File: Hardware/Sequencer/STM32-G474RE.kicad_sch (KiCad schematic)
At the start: 1 part, among them U301 STM32G474RETx

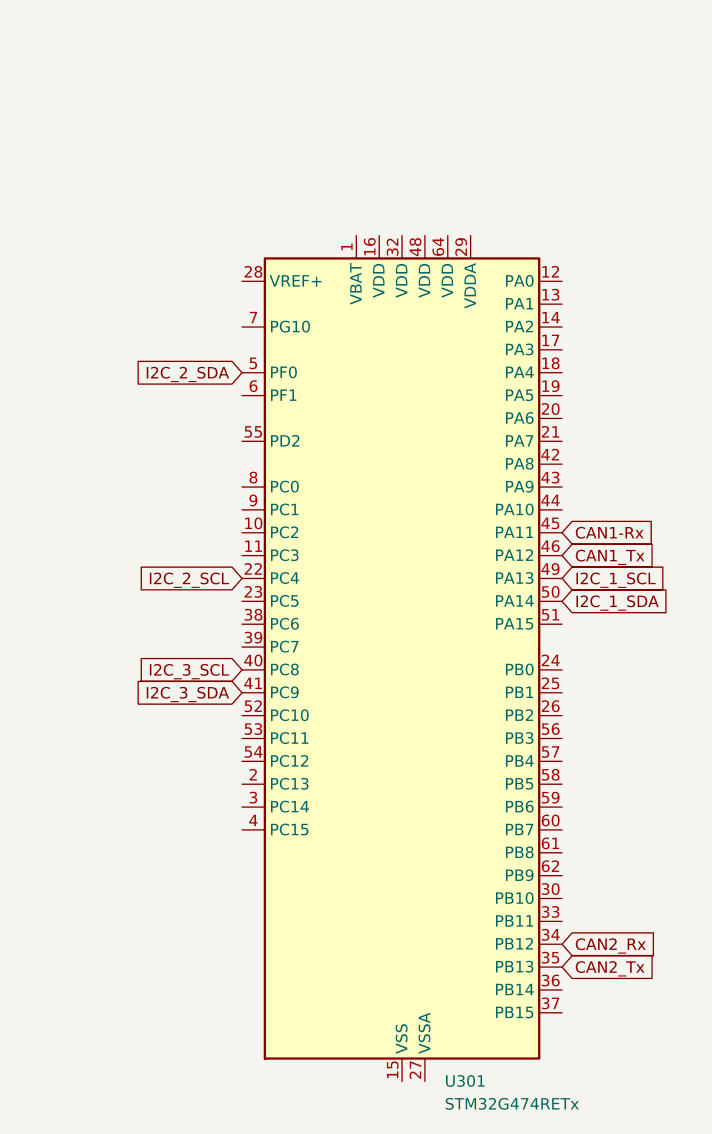
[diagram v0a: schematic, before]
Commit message: Update STM32-G474RE.kicad_sch
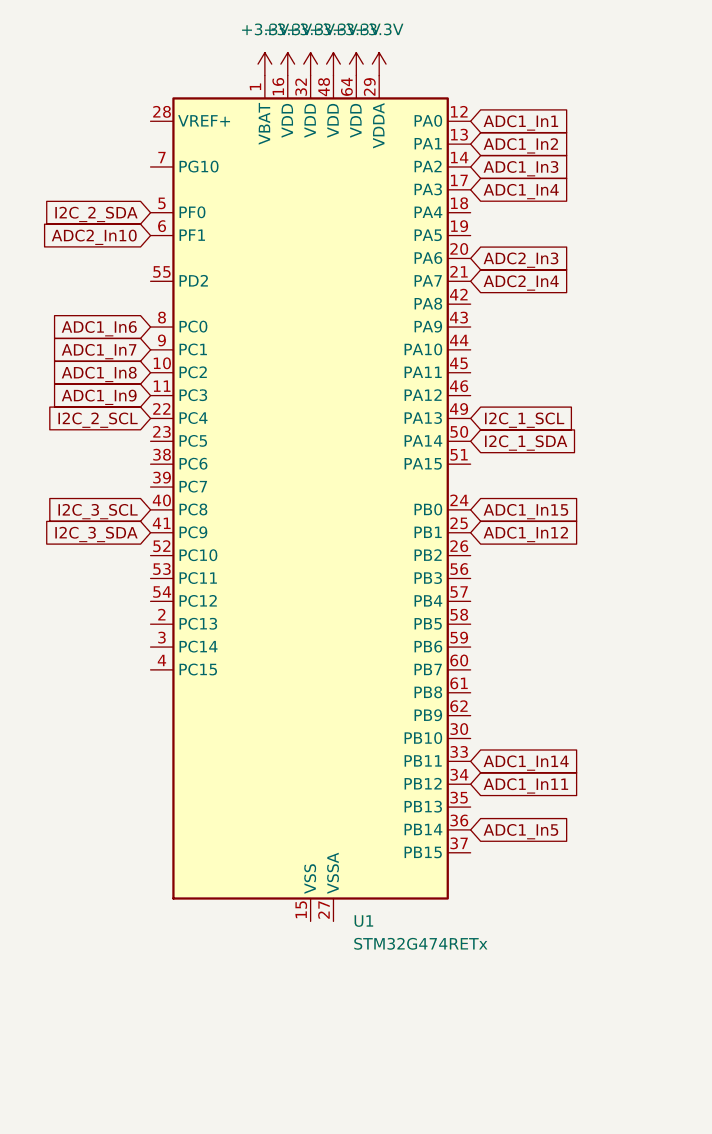
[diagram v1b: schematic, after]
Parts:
- removed U301: STM32G474RETx, Package_QFP:LQFP-64_10x10mm_P0.5mm, symbol MCU_ST_STM32G4:STM32G474RETx
- added U1: STM32G474RETx, Package_QFP:LQFP-64_10x10mm_P0.5mm, symbol MCU_ST_STM32G4:STM32G474RETx
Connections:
- net I2C_1_SCL: now also U1.49 (PA13)
- net I2C_1_SDA: now also U1.50 (PA14)
- net I2C_2_SCL: now also U1.22 (PC4)
- net I2C_2_SDA: now also U1.5 (PF0)
- net I2C_3_SCL: now also U1.40 (PC8)
- net I2C_3_SDA: now also U1.41 (PC9)
- new net: U1.15 (VSS), U1.31 (VSS), U1.47 (VSS), U1.63 (VSS)
- new net +3.3V: U1.1 (VBAT), U1.16 (VDD), U1.29 (VDDA), U1.32 (VDD), U1.48 (VDD), U1.64 (VDD)
- new net ADC1_In1: U1.12 (PA0)
- new net ADC1_In11: U1.34 (PB12)
- new net ADC1_In12: U1.25 (PB1)
- new net ADC1_In14: U1.33 (PB11)
- new net ADC1_In15: U1.24 (PB0)
- new net ADC1_In2: U1.13 (PA1)
- new net ADC1_In3: U1.14 (PA2)
- new net ADC1_In4: U1.17 (PA3)
- new net ADC1_In5: U1.36 (PB14)
- new net ADC1_In6: U1.8 (PC0)
- new net ADC1_In7: U1.9 (PC1)
- new net ADC1_In8: U1.10 (PC2)
- new net ADC1_In9: U1.11 (PC3)
- new net ADC2_In10: U1.6 (PF1)
- new net ADC2_In3: U1.20 (PA6)
- new net ADC2_In4: U1.21 (PA7)

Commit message: Beaucoup de changements sur le pcb
Alim corrigée, ajout de l'USB C

Sonde sur le processeur + linkage USB

Rajout des boutons (465M111...)
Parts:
- added C301, C302, C303, C304, C305, C306, C308: 100n, Capacitor_SMD:C_0402_1005Metric, symbol Device:C_Small
- added C307: 4u7, Capacitor_SMD:C_0402_1005Metric, symbol Device:C_Small
- added J301: Conn_ST_STDC14, Connector_PinHeader_1.27mm:PinHeader_2x07_P1.27mm_Vertical_SMD, symbol Connector:Conn_ST_STDC14
- added SW301: SW_Push, Button_Switch_SMD:SW_Push_1P1T_NO_6x6mm_H9.5mm, symbol Switch:SW_Push
- renumbered U1 to U301
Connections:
- net +3.3V: now also C301.1, C302.1, C303.1, C304.1, C305.1, C306.1, C307.1, J301.3 (VCC)
- net GND: now reaches U301.15 (VSS), U301.31 (VSS), U301.47 (VSS), U301.63 (VSS)
- net GND: now also U301.27 (VSSA), C301.2, C302.2, C303.2, C304.2, C305.2, C306.2, C307.2, C308.2, J301.11 (GNDDetect), J301.5 (GND), J301.7 (GND), SW301.1
- net USB_DM: now reaches U301.45 (PA11)
- net USB_DP: now reaches U301.46 (PA12)
- new net NRST: C308.1, SW301.2
- no-connect marks 0 -> 3

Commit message: pcb
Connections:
- net A2_SID: now reaches U301.2 (PC13)
- net D0: now reaches U301.26 (PB2)
- net A3_SID: now reaches U301.3 (PC14)
- net A4_SID: now reaches U301.4 (PC15)
- net A0_SID: now reaches U301.53 (PC11)
- net A1_SID: now reaches U301.54 (PC12)
- net D1: now reaches U301.56 (PB3)
- net D2: now reaches U301.57 (PB4)
- net D3: now reaches U301.58 (PB5)
- net D4: now reaches U301.59 (PB6)
- net D5: now reaches U301.60 (PB7)
- net D6: now reaches U301.61 (PB8)
- net D7: now reaches U301.62 (PB9)

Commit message: update pcb
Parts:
- added C303, C308: 10n, Capacitor_SMD:C_0402_1005Metric, symbol Device:C_Small
- added D301, D302, D303: LED, LED_SMD:LED_0603_1608Metric, symbol Device:LED
- added R301, R302, R304, R305, R307, R310, R311: 10k, Resistor_SMD:R_0402_1005Metric, symbol Device:R_Small
- added R303: R_Small, Resistor_SMD:R_0402_1005Metric, symbol Device:R_Small
- added R306, R308, R309: 470, Resistor_SMD:R_0402_1005Metric, symbol Device:R_Small
- added SW301, SW302: SW_Push, Button_Switch_SMD:SW_Push_1P1T_NO_6x6mm_H9.5mm, symbol Switch:SW_Push
- renumbered C303 to C304, C304 to C305, C305 to C306, C306 to C307, C307 to C309, C308 to C310, SW301 to SW303
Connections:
- net I2C_1_SCL is gone; now on net SWDIO: U301.49 (PA13)
- net I2C_1_SDA is gone; now on net SWCLK: U301.50 (PA14)
- net I2C_2_SCL is gone; now on net VCP_TX: U301.22 (PC4)
- net NRST is gone; now on net MCO_1MHz: C310.1, SW303.2
- net +3.3V: now also U301.28 (VREF+), R301.1, R302.1, R307.1, R311.1
- net A0_SID: now also U301.44 (PA10); no longer U301.53 (PC11)
- net A1_SID: now also U301.51 (PA15); no longer U301.54 (PC12)
- net A2_SID: now also U301.52 (PC10); no longer U301.2 (PC13)
- net A3_SID: now also U301.53 (PC11); no longer U301.3 (PC14)
- net A4_SID: now also U301.54 (PC12); no longer U301.4 (PC15)
- net D0: now also U301.55 (PD2); no longer U301.26 (PB2)
- net D6: now also R304.1
- net GND: now also C303.2, C308.2, D301.1 (K), D302.1 (K), D303.1 (K), R304.2, R305.2, R307.2, R310.2, R311.2, SW301.1, SW301.2, SW302.1, SW302.2
- net I2C_3_SCL: now also R301.2
- net I2C_3_SDA: now also R302.2
- net MCO_1MHz: now reaches J301.12 (~{RST})
- net MCO_1MHz: now also R303.1
- net VCP_RX: now reaches J301.13 (VCP_RX)
- net VCP_RX: now also U301.23 (PC5)
- net VCP_TX: now reaches J301.14 (VCP_TX)
- net SWDIO: now reaches J301.4 (JTMS/SWDIO)
- net SWCLK: now reaches J301.6 (JCLK/SWCLK)
- net BTN_1: now reaches U301.18 (PA4)
- net BTN_1: now also C303.1, R305.1
- net BTN_2: now reaches U301.19 (PA5)
- net BTN_2: now also C308.1, R310.1
- net INT2_A: now reaches U301.35 (PB13)
- net INT2_B: now reaches U301.37 (PB15)
- net INT1_B: now reaches U301.38 (PC6)
- net INT1_A: now reaches U301.39 (PC7)
- net R/W_SID: now reaches U301.42 (PA8)
- net /RST_SID: now reaches U301.43 (PA9)
- net at U301.7 (PG10): now also R303.2
- net I2C_2_SDA: no longer names the net of U301.5 (PF0)
- new net: D302.2 (A), R308.2
- new net: D301.2 (A), R306.2
- new net: D303.2 (A), R309.2
- new net LED1: R306.1, U301.2 (PC13)
- new net LED2: R308.1, U301.3 (PC14)
- new net LED3: R309.1, U301.4 (PC15)
- new net Tap_Tempo: U301.26 (PB2)
- no-connect marks 3 -> 5
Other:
- moved on the sheet: C310, J301, SW303
